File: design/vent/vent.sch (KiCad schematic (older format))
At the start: 19 parts, among them J10 CS_TEST, J2 OSTYK22102030, J3 SDA_TEST, J4 RX_TEST, J5 TX_TEST, J6 SCL_TEST, J7 SCK_TEST, J8 MISO_TEST, J9 MOSI_TEST

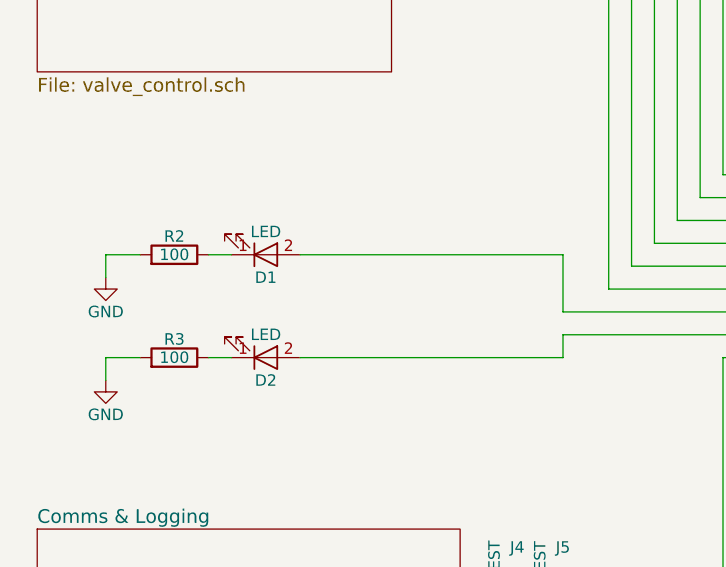
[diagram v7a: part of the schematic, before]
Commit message: Add LED part numbers
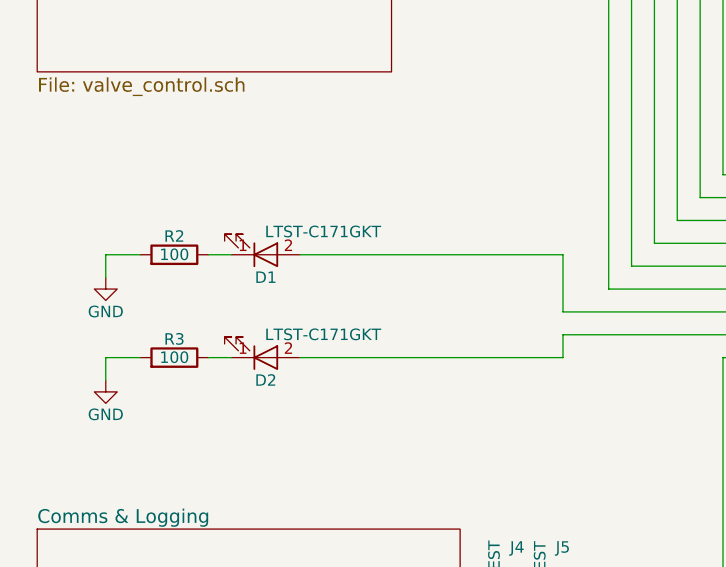
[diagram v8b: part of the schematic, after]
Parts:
- D1, D2: value LED -> LTST-C171GKT
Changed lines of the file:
@@
 P 2600 4200
 F 0 "D1" H 2600 4300 50  0000 C CNN
-F 1 "LED" H 2600 4100 50  0000 C CNN
+F 1 "LTST-C171GKT" H 2850 4100 50  0000 C CNN
 F 2 "LEDs:LED_0805_HandSoldering" H 2600 4200 50  0001 C CNN
 F 3 "" H 2600 4200 50  0001 C CNN
@@
 P 2600 4650
 F 0 "D2" H 2600 4750 50  0000 C CNN
-F 1 "LED" H 2600 4550 50  0000 C CNN
+F 1 "LTST-C171GKT" H 2850 4550 50  0000 C CNN
 F 2 "LEDs:LED_0805_HandSoldering" H 2600 4650 50  0001 C CNN
 F 3 "" H 2600 4650 50  0001 C CNN
